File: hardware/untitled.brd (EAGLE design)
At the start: 47 x 77.8 mm, 63 parts, among them J1 AUDIO_JACK_TRRSSMD_RA, J2 USB4110-GF-A, U1 AT32UC3A1512/1256/1128, U2 USD-SOCKETUSD, U3 LTC3558EUDTRPBFQFN-20_UD_LIT-M

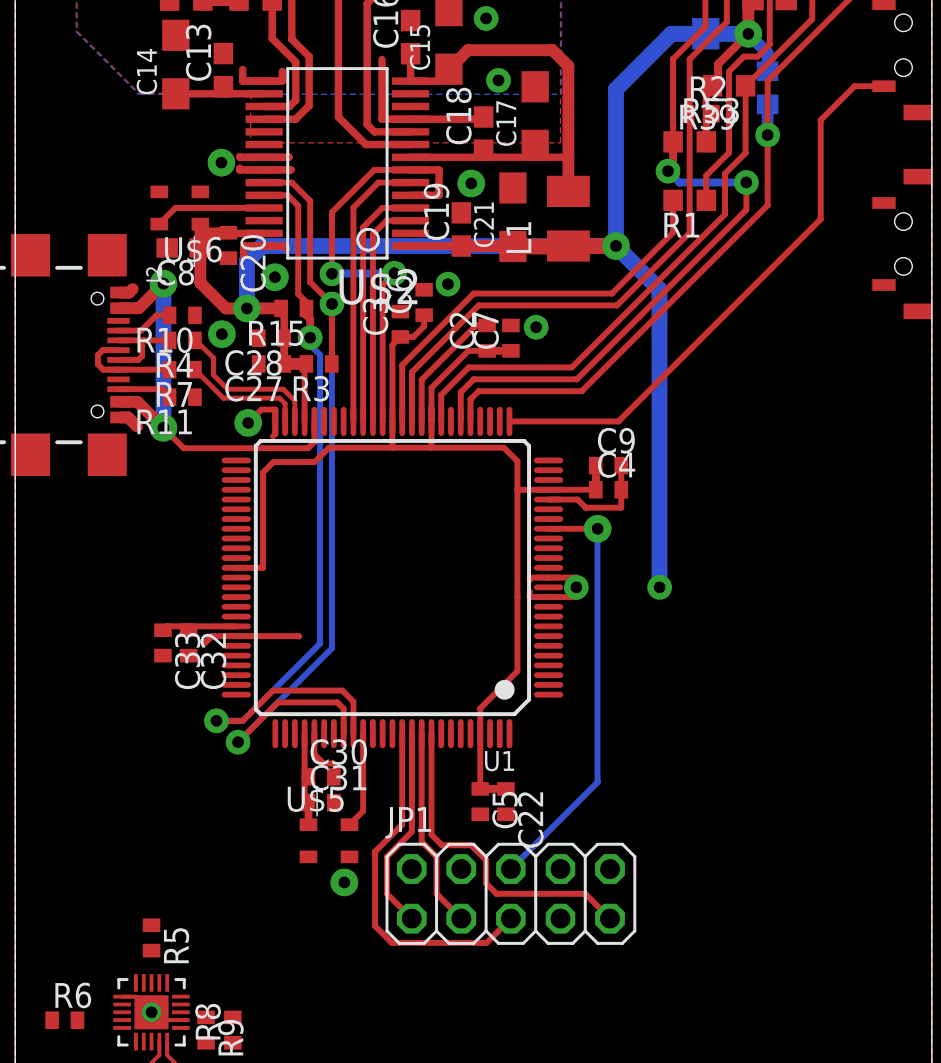
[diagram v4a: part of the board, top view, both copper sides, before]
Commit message: MCU moved right to make place for PMIC
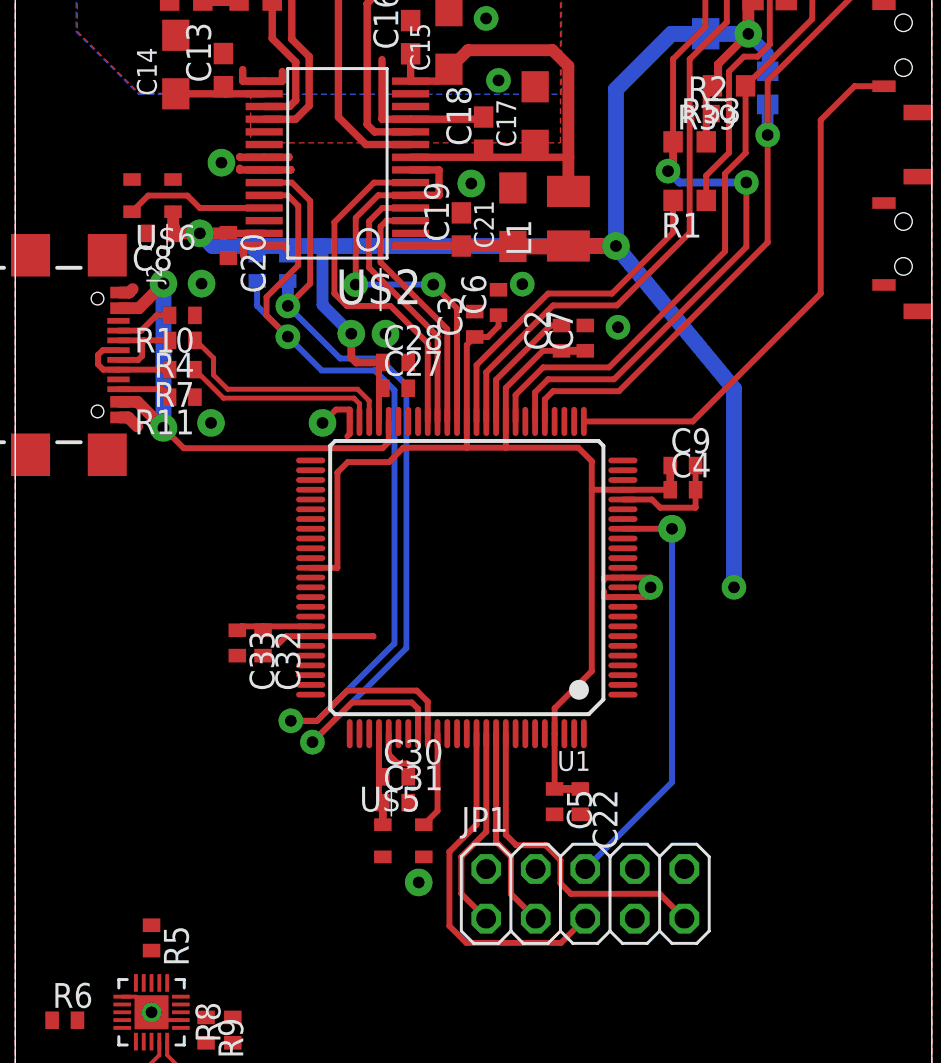
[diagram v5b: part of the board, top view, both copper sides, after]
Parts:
- C8: device rcl:C0603 -> rcl:C0402
- moved C28 6.48 mm to (19.5, 42.8), turned to 0 degrees
- moved C27 6.48 mm to (19.5, 41.5), turned to 0 degrees
- moved R3 5.16 mm to (14.0, 47.7), flipped to the bottom, turned to 90 degrees
- moved C6 3.81 mm to (24.8, 45.9)
- moved C7 3.81 mm to (29.2, 44.1)
- moved JP1 3.81 mm to (29.2, 15.6)
- moved U$5 3.81 mm to (19.9, 18.3)
- moved C30 3.81 mm to (19.5, 21.6)
- moved C31 3.81 mm to (19.5, 20.3)
- moved C33 3.81 mm to (11.4, 28.5)
- moved C2 3.81 mm to (28.0, 44.1)
- moved C22 3.81 mm to (29.0, 20.3)
- moved C3 3.81 mm to (23.5, 44.8)
- moved C32 3.81 mm to (12.7, 28.5)
- moved C4 3.81 mm to (34.2, 36.3)
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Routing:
- net I2C1_SCL: track 41.3 -> 49.4 mm
- net I2S_EXT_SD: track 14.4 -> 18.2 mm
- net VBUS: track 22.3 -> 26.1 mm
- net N$1: track 21.2 -> 17.4 mm
- net D_N: track 7.97 -> 11.8 mm
- net D_P: track 6.25 -> 10.1 mm
- net MOSI: track 34.6 -> 30.7 mm
- net SD_PRESENT: track 36.4 -> 33.7 mm
- net SD_CS: track 37.0 -> 34.3 mm
- net MISO: track 34.3 -> 31.6 mm
- net I2C1_SDA: track 43.7 -> 45.6 mm
- net MCLK: track 5.72 -> 7.38 mm
- net KEY_VOLUP: track 29.3 -> 27.7 mm
- net I2S_SD: track 12.8 -> 14.1 mm
- net I2S_CK: track 11.8 -> 13.1 mm
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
